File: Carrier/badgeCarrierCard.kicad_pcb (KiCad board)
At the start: 4 copper layers, 90 x 145 mm, 144 parts, among them J1 USB_C_Receptacle_USB2.0_16P, J2 MDT420M02003, J3 Conn_01x08, J5 SMA-J-P-X-RA-TH1, J6 1-1734248-5, J7 Conn_01x10, J8 USB_C_Receptacle_USB2.0_16P, J9 Conn_01x30, M1 Z30C1T8460001, Q1 AO3400A, Q2 AO3400A, Q3 AO3400A, Q4 BC847, U1 TCA8418, U10 JDJELECTRONICS_2023_LOGO, U11 TPSGM7227YUWQ10G, U12 USBLC6-2SC6, U15 AP3032, U16 AP3032, U2 IP5306, U3 AMS1117-1.8, U4 ESP32-C6-WROOM-1, U5 Ai-Thinker-Ra-01H, U6 MAX98357A, U7 BME680, U8 BMI270, U9 JDJELECTRONICS_2023_LOGO

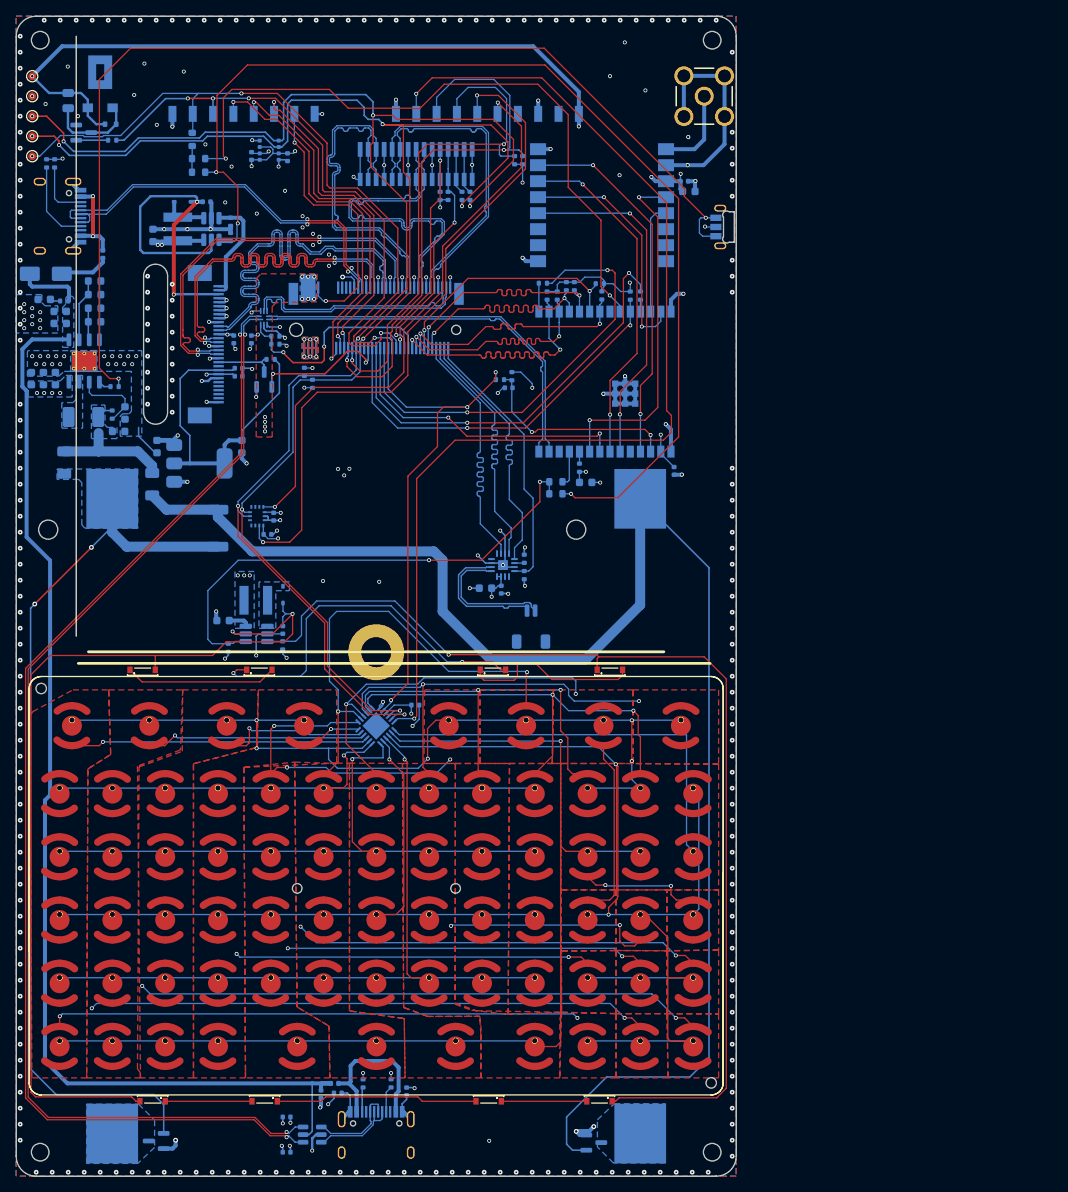
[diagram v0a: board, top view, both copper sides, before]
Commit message: fix: sync schematic prot3 and v2.5
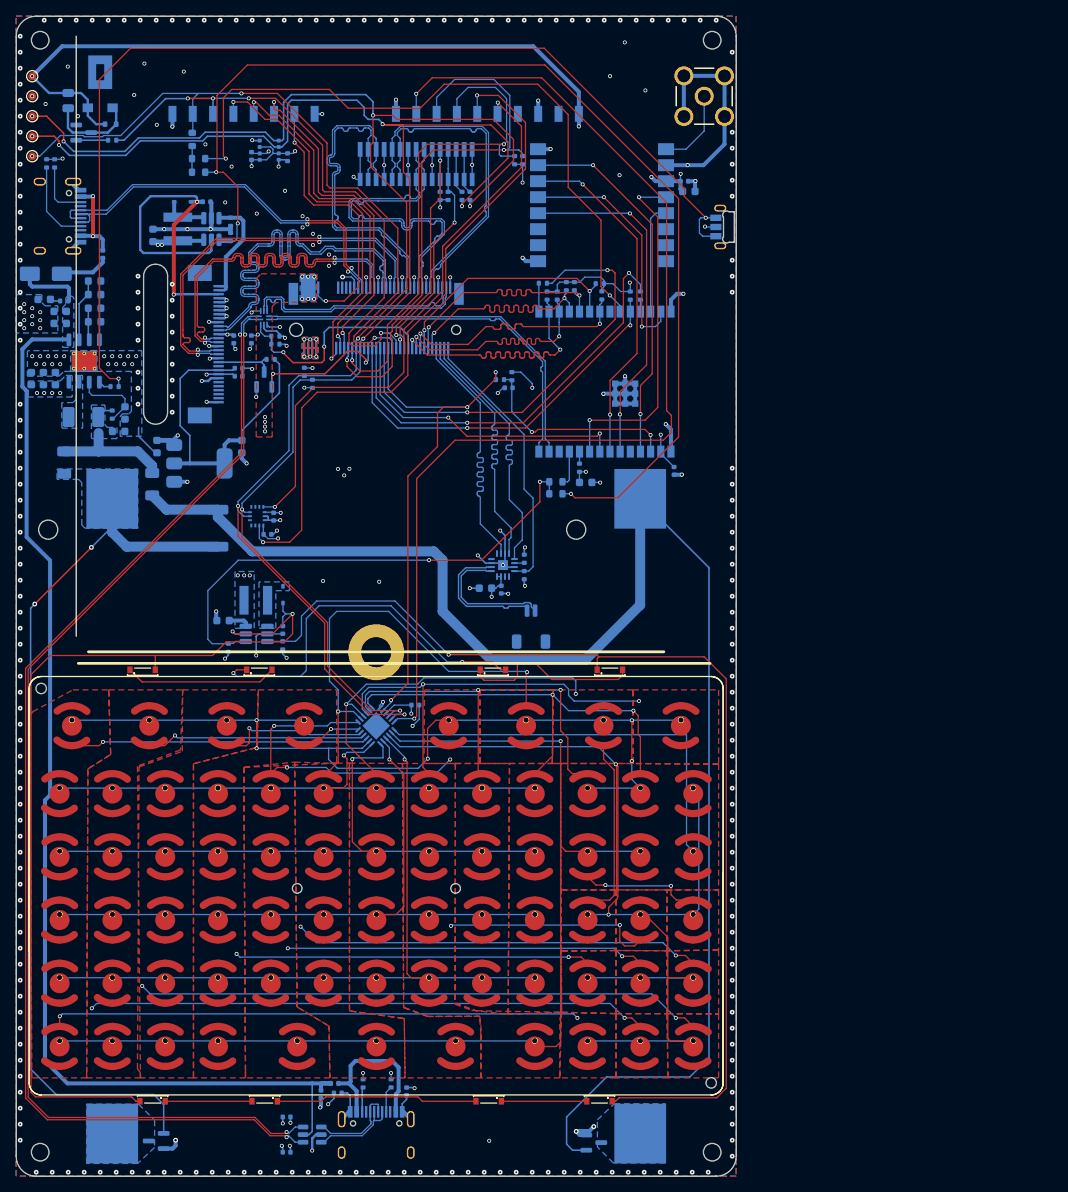
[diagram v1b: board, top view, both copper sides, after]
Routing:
- net /Connectivity (C6 + LoRa)/LoRa/ANTENNA: track 10.7 -> 10.1 mm
- net GND: vias 349 -> 347

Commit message: fix annotation
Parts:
- added C24: 22uF, Capacitor_SMD:C_0603_1608Metric, F.Cu at (146.2, 70.0)
- added C25: 22uF, Capacitor_SMD:C_0603_1608Metric, F.Cu at (146.2, 72.5)
- added C26: 22uF, Capacitor_SMD:C_0603_1608Metric, F.Cu at (146.2, 75.0)
- added D7: LED, LED_SMD:LED_0603_1608Metric, F.Cu at (150.2, 70.0)
- added D8: LED, LED_SMD:LED_0603_1608Metric, F.Cu at (150.2, 72.6)
- added R38: 150, Resistor_SMD:R_0402_1005Metric, F.Cu at (142.7, 69.7)
- added R43: 1K, Resistor_SMD:R_0402_1005Metric, F.Cu at (142.7, 71.7)
- added R46: 470, Resistor_SMD:R_0402_1005Metric, F.Cu at (142.7, 73.7)
- added R47: 150, Resistor_SMD:R_0402_1005Metric, F.Cu at (142.7, 75.7)
- added R48: 1K, Resistor_SMD:R_0402_1005Metric, F.Cu at (142.7, 77.7)
- added R49: 0R, Resistor_SMD:R_0603_1608Metric, F.Cu at (143.2, 83.9)
- added R50: 470, Resistor_SMD:R_0402_1005Metric, F.Cu at (142.7, 79.7)
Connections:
- J2 pad 28: GPIO3 -> /GPIO3
- J2 pad 30: GPIO4 -> /GPIO4
- J3 pad 6: GPIO3 -> /GPIO3
- J3 pad 7: GPIO4 -> /GPIO4
- Q1 pad 1: Net-(BT1-+) -> Net-(Q1-G)
- Q3 pad 1: Net-(BT2-+) -> Net-(Q3-G)
- R16 pad 1: GPIO4 -> /GPIO1
- R37 pad 1: GPIO3 -> /Vibrator/PWM_VIB
- TP5 pad 1: GPIO4 -> /GPIO4
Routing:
- net GPIO4: track 86.9 -> 0.00 mm, vias 3 -> 0
- net /GPIO1: track 43.3 -> 130.2 mm, vias 2 -> 5
- net GPIO3: track 72.9 -> 0.00 mm, vias 4 -> 0
- net (no net): track 0.00 -> 72.9 mm, vias 0 -> 4

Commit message: push back to adam:DDD
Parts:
- added U10: EL817S1C, EL817:SOIC254P1030X390-4N, F.Cu at (153.9, 87.3)
- added U9: EL817S1C, EL817:SOIC254P1030X390-4N, F.Cu at (153.9, 80.9)
